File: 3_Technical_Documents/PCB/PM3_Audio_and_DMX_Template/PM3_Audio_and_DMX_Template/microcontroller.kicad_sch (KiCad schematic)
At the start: 2 parts

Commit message: new push
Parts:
- gave numbers to parts that had none: 2
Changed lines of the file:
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@@
 		(on_board yes)
 		(dnp no)
-		(property "Reference" "#PWR?"
+		(property "Reference" "#PWR017"
 			(at 96.52 116.84 0)
 			(effects
@@
 			(project "PM3_Audio_and_DMX"
 				(path "/1f276d59-ad9b-4e70-a842-f3b7e562eb9b/8b662c4d-5749-4ac0-af71-1d98908dcf56"
-					(reference "#PWR?")
+					(reference "#PWR017")
 					(unit 1)
 				)
@@
 		(on_board yes)
 		(dnp no)
-		(property "Reference" "#PWR?"
+		(property "Reference" "#PWR014"
 			(at 69.85 50.8 0)
 			(effects
@@
 			(project "PM3_Audio_and_DMX"
 				(path "/1f276d59-ad9b-4e70-a842-f3b7e562eb9b/8b662c4d-5749-4ac0-af71-1d98908dcf56"
-					(reference "#PWR?")
+					(reference "#PWR014")
 					(unit 1)
 				)
@@
 		(on_board yes)
 		(dnp no)
-		(property "Reference" "#PWR?"
+		(property "Reference" "#PWR09"
 			(at 30.48 116.84 0)
 			(effects
@@
 			(project "PM3_Audio_and_DMX"
 				(path "/1f276d59-ad9b-4e70-a842-f3b7e562eb9b/8b662c4d-5749-4ac0-af71-1d98908dcf56"
-					(reference "#PWR?")
+					(reference "#PWR09")
 					(unit 1)
 				)
@@
 		(on_board yes)
 		(dnp no)
-		(property "Reference" "#PWR?"
+		(property "Reference" "#PWR013"
 			(at 68.58 116.84 0)
 			(effects
@@
 			(project "PM3_Audio_and_DMX"
 				(path "/1f276d59-ad9b-4e70-a842-f3b7e562eb9b/8b662c4d-5749-4ac0-af71-1d98908dcf56"
-					(reference "#PWR?")
+					(reference "#PWR013")
 					(unit 1)
 				)
@@
 		(on_board yes)
 		(dnp no)
-		(property "Reference" "#PWR?"
+		(property "Reference" "#PWR011"
 			(at 58.42 116.84 0)
 			(effects
@@
 			(project "PM3_Audio_and_DMX"
 				(path "/1f276d59-ad9b-4e70-a842-f3b7e562eb9b/8b662c4d-5749-4ac0-af71-1d98908dcf56"
-					(reference "#PWR?")
+					(reference "#PWR011")
 					(unit 1)
 				)
@@
 		(dnp no)
 		(fields_autoplaced yes)
-		(property "Reference" "P?"
+		(property "Reference" "P1"
 			(at 44.45 31.75 0)
 			(effects
@@
 			(project "PM3_Audio_and_DMX"
 				(path "/1f276d59-ad9b-4e70-a842-f3b7e562eb9b/8b662c4d-5749-4ac0-af71-1d98908dcf56"
-					(reference "P?")
+					(reference "P1")
 					(unit 1)
 				)
@@
 		(on_board yes)
 		(dnp no)
-		(property "Reference" "#PWR?"
+		(property "Reference" "#PWR010"
 			(at 48.26 38.1 0)
 			(effects
@@
 			(project "PM3_Audio_and_DMX"
 				(path "/1f276d59-ad9b-4e70-a842-f3b7e562eb9b/8b662c4d-5749-4ac0-af71-1d98908dcf56"
-					(reference "#PWR?")
+					(reference "#PWR010")
 					(unit 1)
 				)
@@
 		(on_board yes)
 		(dnp no)
-		(property "Reference" "#PWR?"
+		(property "Reference" "#PWR016"
 			(at 86.36 38.1 0)
 			(effects
@@
 			(project "PM3_Audio_and_DMX"
 				(path "/1f276d59-ad9b-4e70-a842-f3b7e562eb9b/8b662c4d-5749-4ac0-af71-1d98908dcf56"
-					(reference "#PWR?")
+					(reference "#PWR016")
 					(unit 1)
 				)
@@
 		(on_board yes)
 		(dnp no)
-		(property "Reference" "#PWR?"
+		(property "Reference" "#PWR015"
 			(at 69.85 73.66 0)
 			(effects
@@
 			(project "PM3_Audio_and_DMX"
 				(path "/1f276d59-ad9b-4e70-a842-f3b7e562eb9b/8b662c4d-5749-4ac0-af71-1d98908dcf56"
-					(reference "#PWR?")
+					(reference "#PWR015")
 					(unit 1)
 				)
@@
 		(on_board yes)
 		(dnp no)
-		(property "Reference" "#PWR?"
+		(property "Reference" "#PWR012"
 			(at 78.74 38.1 0)
 			(effects
@@
 			(project "PM3_Audio_and_DMX"
 				(path "/1f276d59-ad9b-4e70-a842-f3b7e562eb9b/8b662c4d-5749-4ac0-af71-1d98908dcf56"
-					(reference "#PWR?")
+					(reference "#PWR012")
 					(unit 1)
 				)
@@
 		(on_board yes)
 		(dnp no)
-		(property "Reference" "#PWR?"
+		(property "Reference" "#PWR08"
 			(at 40.64 38.1 0)
 			(effects
@@
 			(project "PM3_Audio_and_DMX"
 				(path "/1f276d59-ad9b-4e70-a842-f3b7e562eb9b/8b662c4d-5749-4ac0-af71-1d98908dcf56"
-					(reference "#PWR?")
+					(reference "#PWR08")
 					(unit 1)
 				)
@@
 		(dnp no)
 		(fields_autoplaced yes)
-		(property "Reference" "P?"
+		(property "Reference" "P2"
 			(at 82.55 31.75 0)
 			(effects
@@
 			(project "PM3_Audio_and_DMX"
 				(path "/1f276d59-ad9b-4e70-a842-f3b7e562eb9b/8b662c4d-5749-4ac0-af71-1d98908dcf56"
-					(reference "P?")
-					(unit 1)
-				)
+					(reference "P2")
+					(unit 1)
+				)

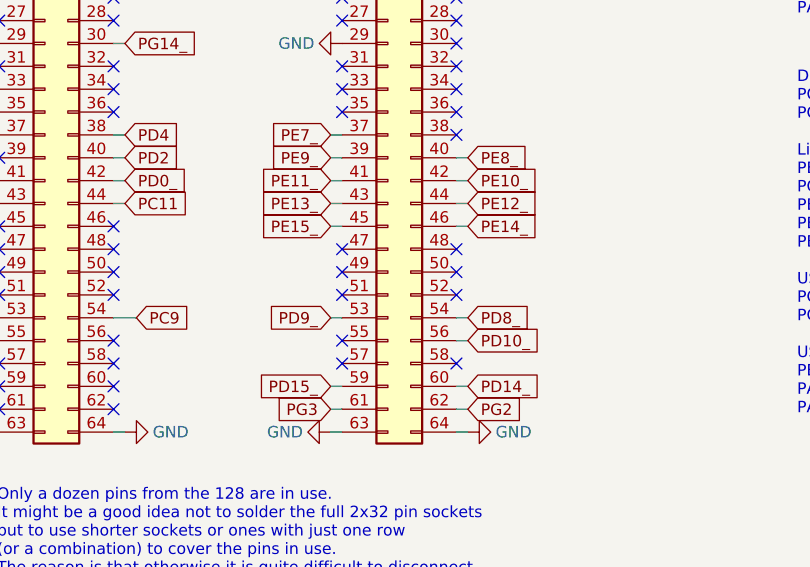
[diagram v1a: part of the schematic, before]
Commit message: i2s added
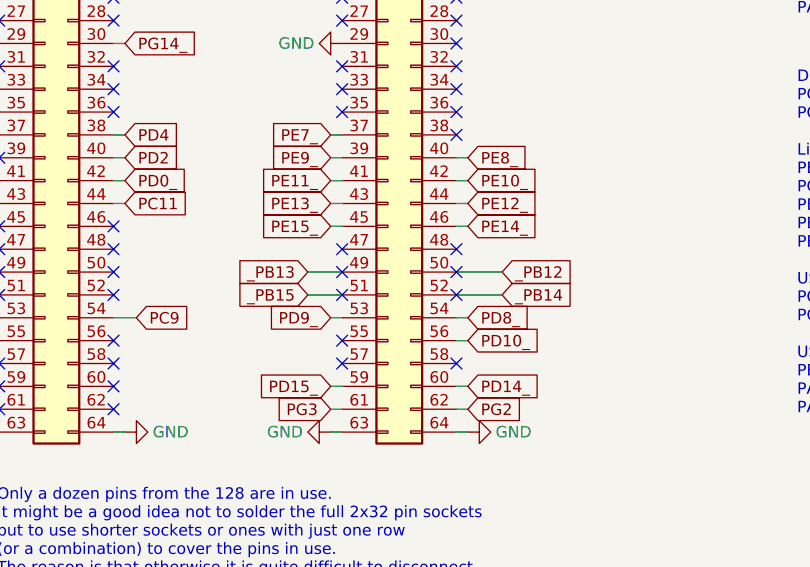
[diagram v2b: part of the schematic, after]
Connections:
- net _PB13: now reaches P2.49 (Pin_49)
- net _PB12: now reaches P2.50 (Pin_50)
- net _PB15: now reaches P2.51 (Pin_51)
- net _PB14: now reaches P2.52 (Pin_52)
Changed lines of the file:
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@@
+	(wire
+		(pts
+			(xy 72.39 101.6) (xy 76.2 101.6)
+		)
+		(stroke
+			(width 0)
+			(type default)
+		)
+	)
 	(wire
 		(pts
@@
 	(wire
 		(pts
+			(xy 72.39 99.06) (xy 76.2 99.06)
+		)
+		(stroke
+			(width 0)
+			(type default)
+		)
+	)
+	(wire
+		(pts
 			(xy 74.93 104.14) (xy 76.2 104.14)
 		)
@@
 	(wire
 		(pts
+			(xy 88.9 99.06) (xy 93.98 99.06)
+		)
+		(stroke
+			(width 0)
+			(type default)
+		)
+	)
+	(wire
+		(pts
 			(xy 36.83 81.28) (xy 38.1 81.28)
 		)
@@
 	(wire
 		(pts
+			(xy 88.9 101.6) (xy 93.98 101.6)
+		)
+		(stroke
+			(width 0)
+			(type default)
+		)
+	)
+	(wire
+		(pts
 			(xy 74.93 38.1) (xy 76.2 38.1)
 		)
@@
 		)
 	)
+	(global_label "_PB12"
+		(shape input)
+		(at 93.98 99.06 0)
+		(fields_autoplaced yes)
+		(effects
+			(font
+				(size 1.27 1.27)
+			)
+			(justify left)
+		)
+		(property "Intersheetrefs" "${INTERSHEET_REFS}"
+			(at 102.8918 99.06 0)
+			(effects
+				(font
+					(size 1.27 1.27)
+				)
+				(justify left)
+				(hide yes)
+			)
+		)
+	)
 	(global_label "PE9_"
 		(shape input)
@@
 		)
 	)
+	(global_label "_PB13"
+		(shape input)
+		(at 72.39 99.06 180)
+		(fields_autoplaced yes)
+		(effects
+			(font
+				(size 1.27 1.27)
+			)
+			(justify right)
+		)
+		(property "Intersheetrefs" "${INTERSHEET_REFS}"
+			(at 63.4782 99.06 0)
+			(effects
+				(font
+					(size 1.27 1.27)
+				)
+				(justify right)
+				(hide yes)
+			)
+		)
+	)
 	(global_label "PA8"
 		(shape input)
@@
 			(effects
 				(font
+					(size 1.27 1.27)
+				)
+				(justify left)
+				(hide yes)
+			)
+		)
+	)
+	(global_label "_PB15"
+		(shape input)
+		(at 72.39 101.6 180)
+		(fields_autoplaced yes)
+		(effects
+			(font
+				(size 1.27 1.27)
+			)
+			(justify right)
+		)
+		(property "Intersheetrefs" "${INTERSHEET_REFS}"
+			(at 63.4782 101.6 0)
+			(effects
+				(font
+					(size 1.27 1.27)
+				)
+				(justify right)
+				(hide yes)
+			)
+		)
+	)
+	(global_label "_PB14"
+		(shape input)
+		(at 93.98 101.6 0)
+		(fields_autoplaced yes)
+		(effects
+			(font
+				(size 1.27 1.27)
+			)
+			(justify left)
+		)
+		(property "Intersheetrefs" "${INTERSHEET_REFS}"
+			(at 102.8918 101.6 0)
+			(effects
+				(font

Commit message: esp-stm connection (+ conflict recolution)
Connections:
- no-connect marks 75 -> 71
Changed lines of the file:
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@@
-	)
-	(no_connect
-		(at 88.9 101.6)
 	)
 	(no_connect
@@
 	)
 	(no_connect
-		(at 76.2 99.06)
-	)
-	(no_connect
-		(at 76.2 101.6)
-	)
-	(no_connect
 		(at 76.2 106.68)
 	)
@@
 	)
 	(no_connect
-		(at 88.9 99.06)
-	)
-	(no_connect
